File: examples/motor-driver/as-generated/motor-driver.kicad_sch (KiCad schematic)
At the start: 12 parts, among them J1 VM 2.7-10.8V, J2 MOTOR A, J3 MOTOR B, J4 LOGIC, U1 DRV8833PW

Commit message: Regenerate the five with stitched pours, silk that speaks, and wires that never double back
All ten variants rebuilt by the fixed generator: reviewed boards carry
ground on both faces with the stitching ring (buck 35 vias, fpga 116),
thru_hole_only front pours, the board id and connector pin names in
silk, and the buck's explicit ground return; the sheets hook power up
through upright symbols and source-anchored flags with no overlapping
wires and no junction-less tees left. Every reviewed variant passes its
own gate with zero errors; every as-generated variant still fails, now
also for the rules this round added.

Co-Authored-By: Claude Fable 5 <noreply@anthropic.com>
Claude-Session: https://claude.ai/code/session_01DUj7Ltu92tWg159mCSacwY
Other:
- moved on the sheet: J1

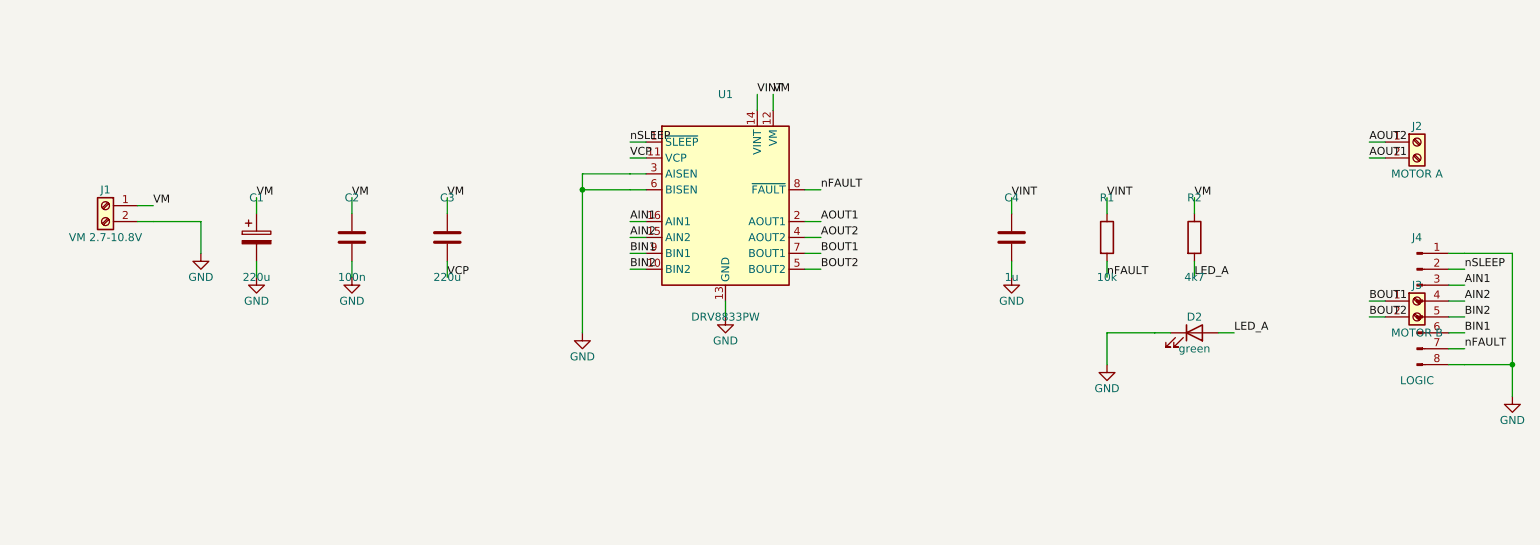
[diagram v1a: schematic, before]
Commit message: Regenerate the five as round three drew them
All five reviewed projects pass their gates again: the buck all wire
with its feedback drawn home, the motor's logic named at the header,
the carrier reading as the pinout table it is - with its feed diode
finally pointing the right way - the filter compact with test points,
and the FPGA's capacitors sitting beside the units they feed. Thirty
renders redrawn, verdict tables at today's numbers.

Co-Authored-By: Claude Fable 5 <noreply@anthropic.com>
Claude-Session: https://claude.ai/code/session_01DUj7Ltu92tWg159mCSacwY
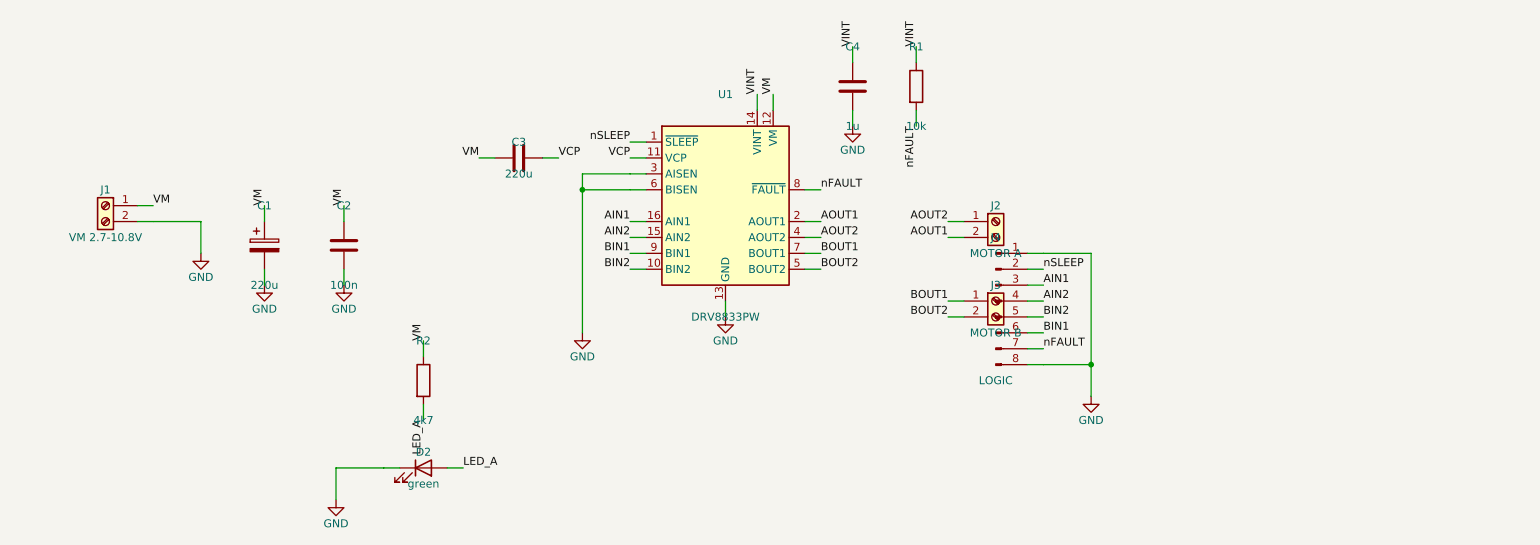
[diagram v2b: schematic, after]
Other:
- moved on the sheet: C1, C2, C3, C4, D2, J2, J3, J4, R1, R2

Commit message: Regenerate the four the text and width work changed
Designators and values off the rails they were printed on, power-named
nets at the width their rule asks for, and the buck's feedback ending
on the capacitor pad it senses at.

Co-Authored-By: Claude Fable 5 <noreply@anthropic.com>
Claude-Session: https://claude.ai/code/session_01DUj7Ltu92tWg159mCSacwY
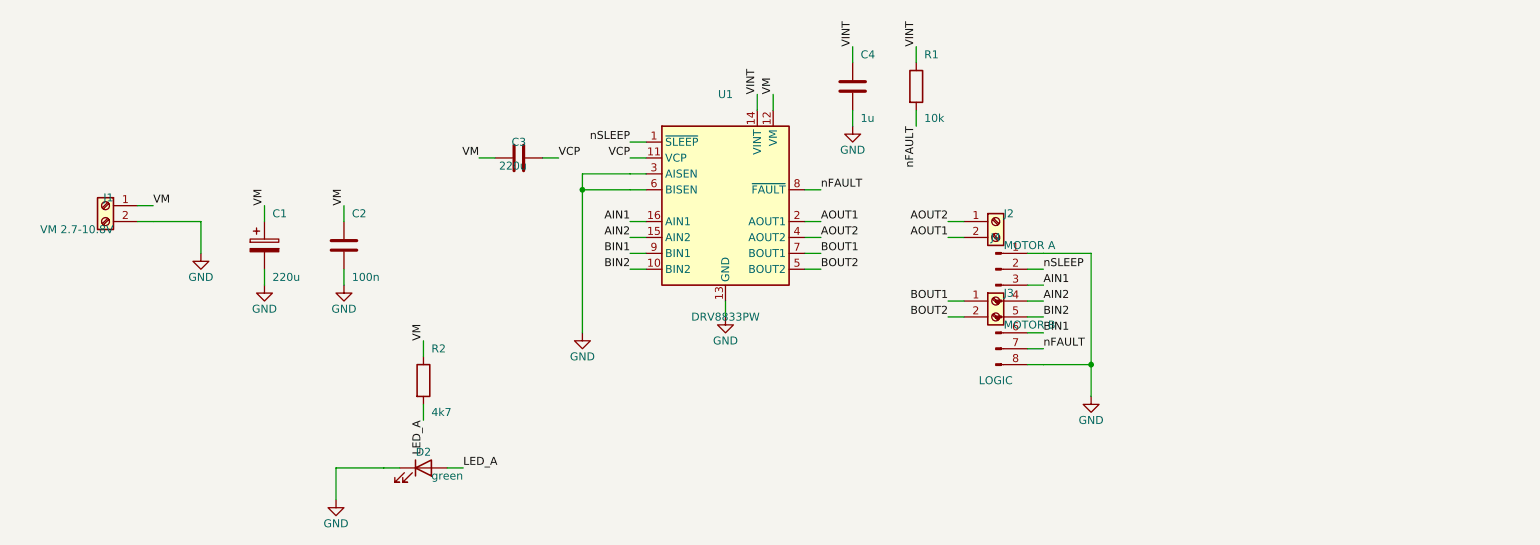
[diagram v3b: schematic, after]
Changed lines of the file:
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@@
   (symbol (lib_id "Connector:Screw_Terminal_01x02") (at 30.79 79.82 0.0) (mirror y) (unit 1)
     (exclude_from_sim no) (in_bom yes) (on_board yes) (dnp no)
-    (property "Reference" "J1" (at 30.79 77.28 0) (effects (font (size 1.27 1.27))))
-    (property "Value" "VM 2.7-10.8V" (at 30.79 84.9 0) (effects (font (size 1.27 1.27))))
+    (property "Reference" "J1" (at 32.06 78.55 0) (effects (font (size 1.27 1.27)) (justify left)))
+    (property "Value" "VM 2.7-10.8V" (at 32.06 83.63 0) (effects (font (size 1.27 1.27)) (justify left)))
     (property "Footprint" "TerminalBlock_Phoenix:TerminalBlock_Phoenix_MKDS-1,5-2_1x02_P5.00mm_Horizontal" (at 30.79 79.82 0) (effects (font (size 1.27 1.27)) hide))
     (property "Datasheet" "https://www.phoenixcontact.com/product/1729128" (at 30.79 79.82 0) (effects (font (size 1.27 1.27)) hide))
@@
   (symbol (lib_id "Device:C_Polarized") (at 56.19 86.17 0.0) (unit 1)
     (exclude_from_sim no) (in_bom yes) (on_board yes) (dnp no)
-    (property "Reference" "C1" (at 56.19 79.82 0) (effects (font (size 1.27 1.27))))
-    (property "Value" "220u" (at 56.19 92.52 0) (effects (font (size 1.27 1.27))))
+    (property "Reference" "C1" (at 57.46 81.09 0) (effects (font (size 1.27 1.27)) (justify left)))
+    (property "Value" "220u" (at 57.46 91.25 0) (effects (font (size 1.27 1.27)) (justify left)))
     (property "Footprint" "Capacitor_SMD:CP_Elec_6.3x7.7" (at 56.19 86.17 0) (effects (font (size 1.27 1.27)) hide))
     (property "Datasheet" "https://industrial.panasonic.com/cdbs/www-data/pdf/RDF0000/ABA0000C1053.pdf" (at 56.19 86.17 0) (effects (font (size 1.27 1.27)) hide))
@@
   (symbol (lib_id "Device:C") (at 68.89 86.17 0.0) (unit 1)
     (exclude_from_sim no) (in_bom yes) (on_board yes) (dnp no)
-    (property "Reference" "C2" (at 68.89 79.82 0) (effects (font (size 1.27 1.27))))
-    (property "Value" "100n" (at 68.89 92.52 0) (effects (font (size 1.27 1.27))))
+    (property "Reference" "C2" (at 70.16 81.09 0) (effects (font (size 1.27 1.27)) (justify left)))
+    (property "Value" "100n" (at 70.16 91.25 0) (effects (font (size 1.27 1.27)) (justify left)))
     (property "Footprint" "Capacitor_SMD:C_0805_2012Metric" (at 68.89 86.17 0) (effects (font (size 1.27 1.27)) hide))
     (property "Datasheet" "https://product.samsungsem.com/mlcc/CL21B104KBCNNNC.do" (at 68.89 86.17 0) (effects (font (size 1.27 1.27)) hide))
@@
     (exclude_from_sim no) (in_bom yes) (on_board yes) (dnp no)
     (property "Reference" "C3" (at 96.83 69.66 90) (effects (font (size 1.27 1.27))))
-    (property "Value" "220u" (at 96.83 74.74 90) (effects (font (size 1.27 1.27))))
+    (property "Value" "220u" (at 98.1 73.47 90) (effects (font (size 1.27 1.27)) (justify left)))
     (property "Footprint" "Capacitor_SMD:C_0805_2012Metric" (at 96.83 72.2 0) (effects (font (size 1.27 1.27)) hide))
     (property "Datasheet" "https://product.samsungsem.com/mlcc/CL21B103KBANNNC.do" (at 96.83 72.2 0) (effects (font (size 1.27 1.27)) hide))
@@
   (symbol (lib_id "Device:C") (at 150.17 60.77 0.0) (unit 1)
     (exclude_from_sim no) (in_bom yes) (on_board yes) (dnp no)
-    (property "Reference" "C4" (at 150.17 54.42 0) (effects (font (size 1.27 1.27))))
-    (property "Value" "1u" (at 150.17 67.12 0) (effects (font (size 1.27 1.27))))
+    (property "Reference" "C4" (at 151.44 55.69 0) (effects (font (size 1.27 1.27)) (justify left)))
+    (property "Value" "1u" (at 151.44 65.85 0) (effects (font (size 1.27 1.27)) (justify left)))
     (property "Footprint" "Capacitor_SMD:C_0805_2012Metric" (at 150.17 60.77 0) (effects (font (size 1.27 1.27)) hide))
     (property "Datasheet" "https://product.samsungsem.com/mlcc/CL21A105KBFNNNE.do" (at 150.17 60.77 0) (effects (font (size 1.27 1.27)) hide))
@@
   (symbol (lib_id "Device:R") (at 160.33 60.77 0.0) (unit 1)
     (exclude_from_sim no) (in_bom yes) (on_board yes) (dnp no)
-    (property "Reference" "R1" (at 160.33 54.42 0) (effects (font (size 1.27 1.27))))
-    (property "Value" "10k" (at 160.33 67.12 0) (effects (font (size 1.27 1.27))))
+    (property "Reference" "R1" (at 161.6 55.69 0) (effects (font (size 1.27 1.27)) (justify left)))
+    (property "Value" "10k" (at 161.6 65.85 0) (effects (font (size 1.27 1.27)) (justify left)))
     (property "Footprint" "Resistor_SMD:R_0805_2012Metric" (at 160.33 60.77 0) (effects (font (size 1.27 1.27)) hide))
     (property "Datasheet" "https://www.yageo.com/upload/media/product/productsearch/datasheet/rchip/PYu-RC_Group_51_RoHS_L_12.pdf" (at 160.33 60.77 0) (effects (font (size 1.27 1.27)) hide))
@@
   (symbol (lib_id "Device:R") (at 81.59 107.76 0.0) (unit 1)
     (exclude_from_sim no) (in_bom yes) (on_board yes) (dnp no)
-    (property "Reference" "R2" (at 81.59 101.41 0) (effects (font (size 1.27 1.27))))
-    (property "Value" "4k7" (at 81.59 114.11 0) (effects (font (size 1.27 1.27))))
+    (property "Reference" "R2" (at 82.86 102.68 0) (effects (font (size 1.27 1.27)) (justify left)))
+    (property "Value" "4k7" (at 82.86 112.84 0) (effects (font (size 1.27 1.27)) (justify left)))
     (property "Footprint" "Resistor_SMD:R_0805_2012Metric" (at 81.59 107.76 0) (effects (font (size 1.27 1.27)) hide))
     (property "Datasheet" "https://www.yageo.com/upload/media/product/productsearch/datasheet/rchip/PYu-RC_Group_51_RoHS_L_12.pdf" (at 81.59 107.76 0) (effects (font (size 1.27 1.27)) hide))
@@
     (exclude_from_sim no) (in_bom yes) (on_board yes) (dnp no)
     (property "Reference" "D2" (at 81.59 119.19 0) (effects (font (size 1.27 1.27))))
-    (property "Value" "green" (at 81.59 124.27 0) (effects (font (size 1.27 1.27))))
+    (property "Value" "green" (at 82.86 123.0 0) (effects (font (size 1.27 1.27)) (justify left)))
     (property "Footprint" "LED_SMD:LED_0805_2012Metric" (at 81.59 121.73 0) (effects (font (size 1.27 1.27)) hide))
     (property "Datasheet" "https://optoelectronics.liteon.com/upload/download/DS-22-98-0002/LTST-C170KGKT.pdf" (at 81.59 121.73 0) (effects (font (size 1.27 1.27)) hide))
@@
   (symbol (lib_id "Connector:Screw_Terminal_01x02") (at 173.03 82.36 0.0) (unit 1)
     (exclude_from_sim no) (in_bom yes) (on_board yes) (dnp no)
-    (property "Reference" "J2" (at 173.03 79.82 0) (effects (font (size 1.27 1.27))))
-    (property "Value" "MOTOR A" (at 173.03 87.44 0) (effects (font (size 1.27 1.27))))
+    (property "Reference" "J2" (at 174.3 81.09 0) (effects (font (size 1.27 1.27)) (justify left)))
+    (property "Value" "MOTOR A" (at 174.3 86.17 0) (effects (font (size 1.27 1.27)) (justify left)))
     (property "Footprint" "TerminalBlock_Phoenix:TerminalBlock_Phoenix_MKDS-1,5-2_1x02_P5.00mm_Horizontal" (at 173.03 82.36 0) (effects (font (size 1.27 1.27)) hide))
     (property "Datasheet" "https://www.phoenixcontact.com/product/1729128" (at 173.03 82.36 0) (effects (font (size 1.27 1.27)) hide))
@@
   (symbol (lib_id "Connector:Screw_Terminal_01x02") (at 173.03 95.06 0.0) (unit 1)
     (exclude_from_sim no) (in_bom yes) (on_board yes) (dnp no)
-    (property "Reference" "J3" (at 173.03 92.52 0) (effects (font (size 1.27 1.27))))
-    (property "Value" "MOTOR B" (at 173.03 100.14 0) (effects (font (size 1.27 1.27))))
+    (property "Reference" "J3" (at 174.3 93.79 0) (effects (font (size 1.27 1.27)) (justify left)))
+    (property "Value" "MOTOR B" (at 174.3 98.87 0) (effects (font (size 1.27 1.27)) (justify left)))
     (property "Footprint" "TerminalBlock_Phoenix:TerminalBlock_Phoenix_MKDS-1,5-2_1x02_P5.00mm_Horizontal" (at 173.03 95.06 0) (effects (font (size 1.27 1.27)) hide))
     (property "Datasheet" "https://www.phoenixcontact.com/product/1729128" (at 173.03 95.06 0) (effects (font (size 1.27 1.27)) hide))
